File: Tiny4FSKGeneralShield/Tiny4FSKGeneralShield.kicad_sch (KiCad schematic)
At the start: 33 parts, among them J1 Micro_SD_Card, J10 Ext.IMU, J11 Ext.Photo, J12 Int.OLED, J15 Int.Pwr, J16 3v3 IO, J17 5V IO, J2 USB_C_Receptacle_USB2.0_14P, J3 TinyI2C, J4 TinyGPIO, J5 Ext.BME280, J6 TinySPI, J7 TinyPwr, J8 TinyUSB, J9 Ext.Pwr, U1 FXMA108, U3 TPS63060

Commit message: ugh it got overwritten
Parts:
- C3: footprint Capacitor_SMD:C_0805_2012Metric -> Capacitor_SMD:C_0402_1005Metric; JLCPCB Part # (none) -> C1525
- C4: footprint Capacitor_SMD:C_0805_2012Metric -> Capacitor_SMD:C_0402_1005Metric; JLCPCB Part # (none) -> C32949
- C5, C6: footprint Capacitor_SMD:C_0805_2012Metric -> Capacitor_SMD:C_0402_1005Metric; JLCPCB Part # (none) -> C15525
- C7, C8, C9: footprint Capacitor_SMD:C_0805_2012Metric -> Capacitor_SMD:C_0603_1608Metric; JLCPCB Part # (none) -> C59461
- J1: footprint Connector_Card:microSD_HC_Hirose_DM3D-SF -> TF-PUSH:TF-PUSH; symbol Connector:Micro_SD_Card -> Connector:Micro_SD_Card_Det1; JLCPCB Part # (none) -> C393941
- J2: JLCPCB Part # (none) -> C2760486
- L1: JLCPCB Part # (none) -> C842935
- R1, R2: value 5k1 -> 5.1kR; footprint Resistor_SMD:R_0805_2012Metric -> Resistor_SMD:R_0402_1005Metric; JLCPCB Part # (none) -> C25905
- R3, R5: value 1k -> 1kR; footprint Resistor_SMD:R_0805_2012Metric -> Resistor_SMD:R_0402_1005Metric; JLCPCB Part # (none) -> C11702
- R4, R6: value 2k -> 2kR; footprint Resistor_SMD:R_0805_2012Metric -> Resistor_SMD:R_0402_1005Metric; JLCPCB Part # (none) -> C4109
- R7: footprint Resistor_SMD:R_0805_2012Metric -> Resistor_SMD:R_0402_1005Metric; JLCPCB Part # (none) -> C26083
- R9: value 111k -> 111kR; JLCPCB Part # (none) -> C865144
- U1: JLCPCB Part # (none) -> C891320
- U3: JLCPCB Part # (none) -> C48567
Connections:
- net +3.3V: now also J12.3 (Pin_3); no longer J12.1 (Pin_1)
- net Earth: now also J12.4 (Pin_4); no longer J1.11 (SHIELD), J1.9 (SHIELD), J12.2 (Pin_2)
- net SCL: now also J12.2 (Pin_2); no longer J12.3 (Pin_3)
- net SDA: now also J12.1 (Pin_1); no longer J12.4 (Pin_4)
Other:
- moved on the sheet: J12

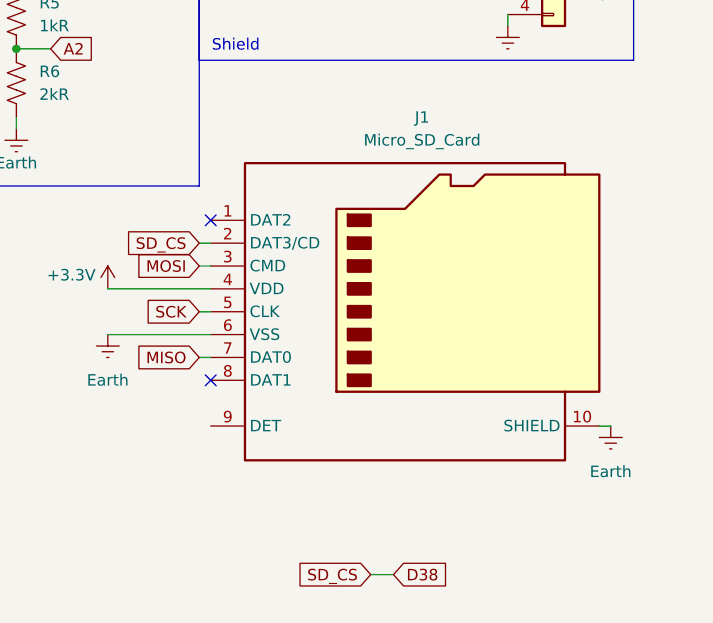
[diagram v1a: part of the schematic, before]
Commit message: need to find jlc part for qwiic
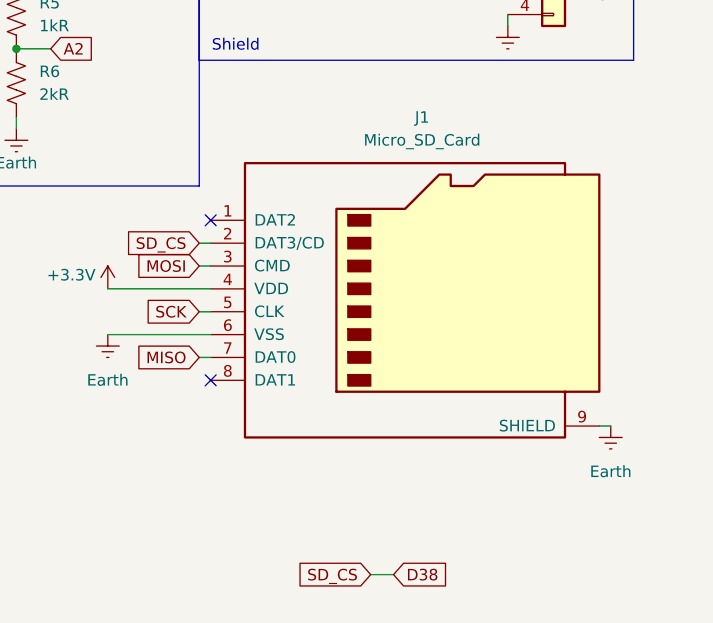
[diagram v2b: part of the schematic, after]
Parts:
- J1: footprint TF-PUSH:TF-PUSH -> Connector_Card:microSD_HC_Hirose_DM3D-SF; symbol Connector:Micro_SD_Card_Det1 -> Connector:Micro_SD_Card; JLCPCB Part # C393941 -> C719027
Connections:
- net Earth: now also J1.9 (SHIELD); no longer J1.10 (SHIELD)
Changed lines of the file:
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@@
 	(wire
 		(pts
+			(xy 236.22 92.71) (xy 234.95 92.71)
+		)
+		(stroke
+			(width 0)
+			(type default)
+		)
+	)
+	(wire
+		(pts
 			(xy 199.39 31.75) (xy 200.66 31.75)
 		)
@@
 	(wire
 		(pts
+			(xy 236.22 102.87) (xy 234.95 102.87)
+		)
+		(stroke
+			(width 0)
+			(type default)
+		)
+	)
+	(wire
+		(pts
 			(xy 49.53 53.34) (xy 64.77 53.34)
 		)
@@
 	(wire
 		(pts
-			(xy 113.03 97.79) (xy 100.33 97.79)
+			(xy 224.79 95.25) (xy 236.22 95.25)
 		)
 		(stroke
@@
 	(wire
 		(pts
-			(xy 245.11 22.86) (xy 246.38 22.86)
+			(xy 113.03 97.79) (xy 100.33 97.79)
 		)
 		(stroke
@@
 	(wire
 		(pts
-			(xy 224.79 100.33) (xy 236.22 100.33)
+			(xy 245.11 22.86) (xy 246.38 22.86)
 		)
 		(stroke
@@
 	(wire
 		(pts
+			(xy 236.22 90.17) (xy 234.95 90.17)
+		)
+		(stroke
+			(width 0)
+			(type default)
+		)
+	)
+	(wire
+		(pts
 			(xy 57.15 38.1) (xy 53.34 38.1)
 		)
@@
 	(wire
 		(pts
-			(xy 236.22 102.87) (xy 234.95 102.87)
+			(xy 35.56 68.58) (xy 38.1 68.58)
 		)
 		(stroke
@@
 	(wire
 		(pts
-			(xy 35.56 68.58) (xy 38.1 68.58)
+			(xy 100.33 107.95) (xy 113.03 107.95)
 		)
 		(stroke
@@
 	(wire
 		(pts
-			(xy 100.33 107.95) (xy 113.03 107.95)
+			(xy 208.28 17.78) (xy 208.28 19.05)
 		)
 		(stroke
@@
 	(wire
 		(pts
-			(xy 208.28 17.78) (xy 208.28 19.05)
+			(xy 87.63 83.82) (xy 86.36 83.82)
 		)
 		(stroke
@@
 	(wire
 		(pts
-			(xy 87.63 83.82) (xy 86.36 83.82)
+			(xy 53.34 38.1) (xy 53.34 39.37)
 		)
 		(stroke
@@
 	(wire
 		(pts
-			(xy 53.34 38.1) (xy 53.34 39.37)
+			(xy 36.83 93.98) (xy 38.1 93.98)
 		)
 		(stroke
@@
 	(wire
 		(pts
-			(xy 36.83 93.98) (xy 38.1 93.98)
+			(xy 78.74 35.56) (xy 77.47 35.56)
 		)
 		(stroke
@@
 	(wire
 		(pts
-			(xy 78.74 35.56) (xy 77.47 35.56)
+			(xy 236.22 97.79) (xy 234.95 97.79)
 		)
 		(stroke
@@
 	(wire
 		(pts
-			(xy 236.22 90.17) (xy 234.95 90.17)
-		)
-		(stroke
-			(width 0)
-			(type default)
-		)
-	)
-	(wire
-		(pts
-			(xy 236.22 97.79) (xy 234.95 97.79)
-		)
-		(stroke
-			(width 0)
-			(type default)
-		)
-	)
-	(wire
-		(pts
 			(xy 199.39 39.37) (xy 200.66 39.37)
 		)
@@
 	(wire
 		(pts
-			(xy 224.79 95.25) (xy 236.22 95.25)
-		)
-		(stroke
-			(width 0)
-			(type default)
-		)
-	)
-	(wire
-		(pts
 			(xy 256.54 127) (xy 254 127)
 		)
@@
 	(wire
 		(pts
-			(xy 236.22 92.71) (xy 234.95 92.71)
-		)
-		(stroke
-			(width 0)
-			(type default)
-		)
-	)
-	(wire
-		(pts
 			(xy 162.56 33.02) (xy 161.29 33.02)
 		)
@@
 	(wire
 		(pts
+			(xy 224.79 100.33) (xy 236.22 100.33)
+		)
+		(stroke
+			(width 0)
+			(type default)
+		)
+	)
+	(wire
+		(pts
 			(xy 69.85 135.89) (xy 71.12 135.89)
 		)
@@
 	)
 	(symbol
-		(lib_id "Connector:Micro_SD_Card_Det1")
-		(at 259.08 97.79 0)
+		(lib_id "Connector:Micro_SD_Card")
+		(at 259.08 95.25 0)
 		(unit 1)
 		(body_style 1)
@@
 			)
 		)
-		(property "Footprint" "TF-PUSH:TF-PUSH"
-			(at 311.15 80.01 0)
+		(property "Footprint" "Connector_Card:microSD_HC_Hirose_DM3D-SF"
+			(at 288.29 87.63 0)
 			(hide yes)
 			(effects
@@
 			)
 		)
-		(property "Datasheet" "https://datasheet.lcsc.com/lcsc/2110151630_XKB-Connectivity-XKTF-015-N_C381082.pdf"
+		(property "Datasheet" "https://www.we-online.com/components/products/datasheet/693072010801.pdf"
 			(at 259.08 95.25 0)
 			(hide yes)
@@
 			)
 		)
-		(property "Description" "Micro SD Card Socket with one card detection pin"
-			(at 259.08 97.79 0)
+		(property "Description" "Micro SD Card Socket"
+			(at 259.08 95.25 0)
 			(hide yes)
 			(effects
@@
 			)
 		)
-		(property "JLCPCB Part #" "C393941"
-			(at 259.08 97.79 0)
+		(property "JLCPCB Part #" "C719027"
+			(at 259.08 95.25 0)
 			(hide yes)
 			(effects
@@
 		(pin "9"
 		)
-		(pin "10"
-		)
 		(instances

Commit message: release candidate!
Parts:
- J10: JLCPCB Part # (none) -> C160405
- J11: JLCPCB Part # (none) -> C160402
- J5: JLCPCB Part # (none) -> C51940130
- J9: footprint Connector_Molex:Molex_PicoBlade_53261-0271_1x02-1MP_P1.25mm_Horizontal -> Connector_JSt_Extended:HX20007-2AWB; JLCPCB Part # (none) -> C442222
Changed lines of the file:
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@@
 	(wire
 		(pts
-			(xy 35.56 68.58) (xy 38.1 68.58)
+			(xy 24.13 68.58) (xy 38.1 68.58)
 		)
 		(stroke
@@
 			)
 		)
-		(property "Footprint" "Connector_Molex:Molex_PicoBlade_53261-0271_1x02-1MP_P1.25mm_Horizontal"
+		(property "Footprint" "Connector_JSt_Extended:HX20007-2AWB"
 			(at 43.18 121.92 0)
 			(hide yes)
@@
 			)
 		)
-		(property "JLCPCB Part #" ""
+		(property "JLCPCB Part #" "C442222"
 			(at 43.18 121.92 0)
 			(hide yes)
@@
 			)
 		)
-		(property "JLCPCB Part #" ""
+		(property "JLCPCB Part #" "C160402"
 			(at 43.18 107.95 0)
 			(hide yes)
@@
 			)
 		)
-		(property "JLCPCB Part #" ""
+		(property "JLCPCB Part #" "C51940130"
 			(at 43.18 71.12 0)
 			(hide yes)
@@
 	(symbol
 		(lib_id "power:Earth")
-		(at 35.56 68.58 180)
+		(at 24.13 68.58 0)
 		(unit 1)
 		(body_style 1)
@@
 		(dnp no)
 		(property "Reference" "#PWR027"
-			(at 35.56 62.23 0)
+			(at 24.13 74.93 0)
 			(hide yes)
 			(effects
@@
 		)
 		(property "Value" "Earth"
-			(at 35.56 64.516 0)
+			(at 24.13 72.644 0)
 			(effects
 				(font
@@
 		)
 		(property "Footprint" ""
-			(at 35.56 68.58 0)
+			(at 24.13 68.58 0)
 			(hide yes)
 			(effects
@@
 		)
 		(property "Datasheet" ""
-			(at 35.56 68.58 0)
+			(at 24.13 68.58 0)
 			(hide yes)
 			(effects
@@
 		)
 		(property "Description" "Power symbol creates a global label with name \"Earth\""
-			(at 35.56 68.58 0)
+			(at 24.13 68.58 0)
 			(hide yes)
 			(effects
@@
 			)
 		)
-		(property "JLCPCB Part #" ""
+		(property "JLCPCB Part #" "C160405"
 			(at 43.18 91.44 0)
 			(hide yes)
